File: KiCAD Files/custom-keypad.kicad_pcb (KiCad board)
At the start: 2 copper layers, 67.8 x 65.5 mm, 40 parts, among them IC1 AZ1117IH-3.3TRG1, IC2 USBLC6-2SC6, J1 UJ32-C-H-G-H2-SMT-TR, J2 EN11-HSM1BF20, J3 61300511121, SW1 SW_Push, SW2 SW_Push, SW3 SW_Push, SW4 SW_Push, SW8 SW_Push, SW9 SW_Push, U1 STM32H7A3RGTx, Y1 LFXTAL010595

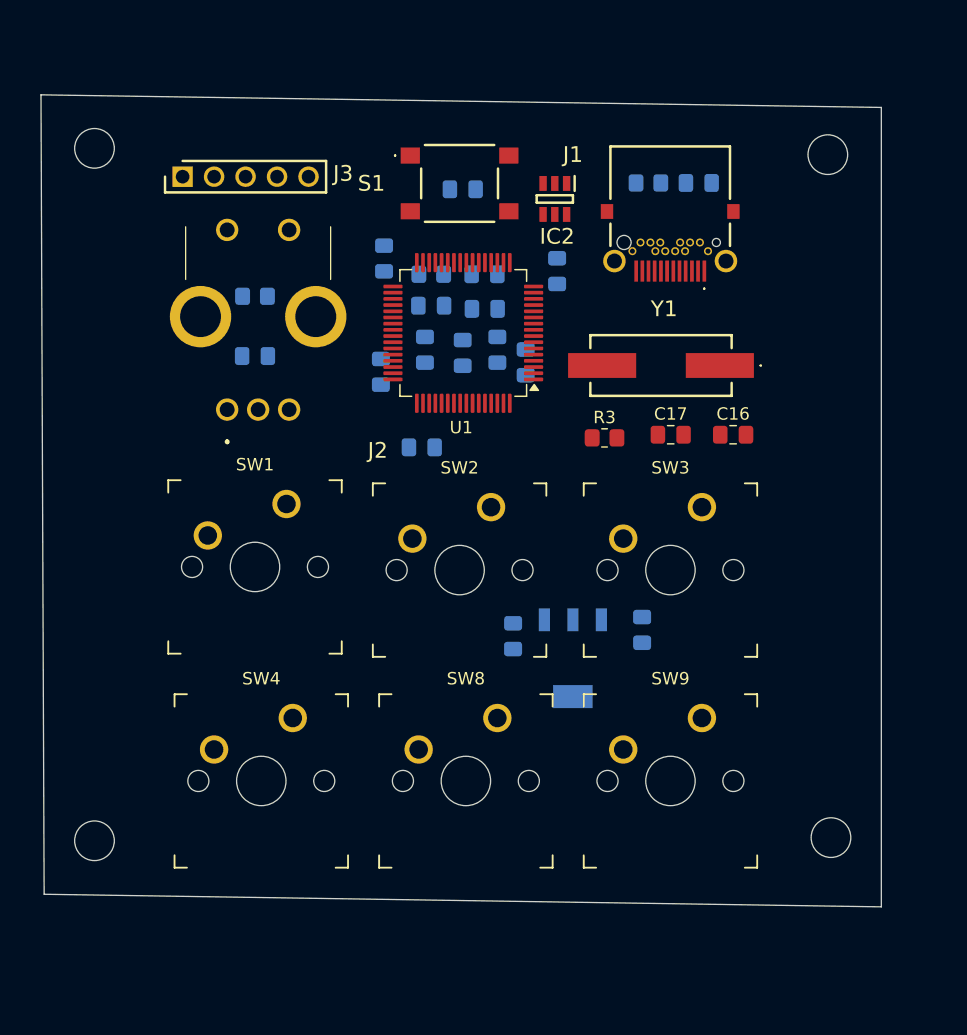
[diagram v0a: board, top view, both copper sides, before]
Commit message: improved PCB design and added debugging circuitry
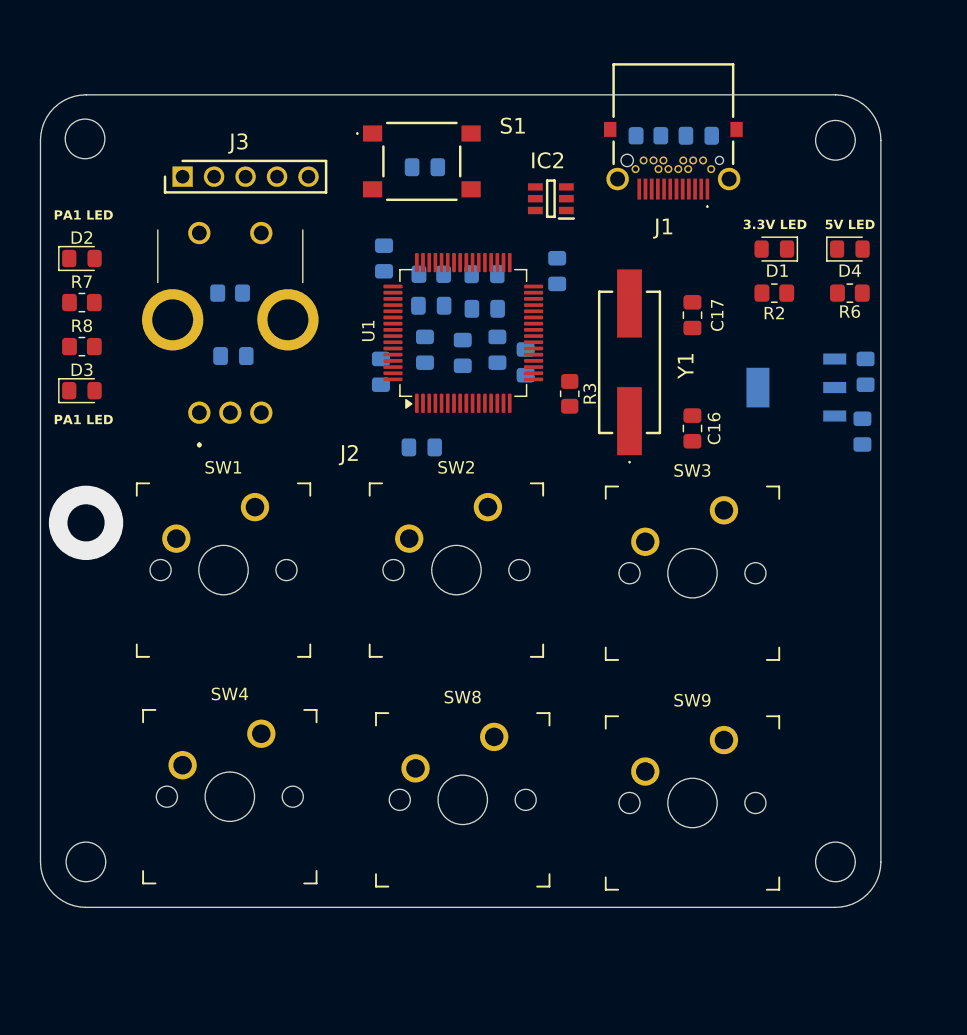
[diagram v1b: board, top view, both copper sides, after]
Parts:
- added D1: LED, LED_SMD:LED_0805_2012Metric_Pad1.15x1.40mm_HandSolder, F.Cu at (110.5, 38.1)
- added D2: LED, LED_SMD:LED_0805_2012Metric_Pad1.15x1.40mm_HandSolder, F.Cu at (54.6, 38.9)
- added D3: LED, LED_SMD:LED_0805_2012Metric_Pad1.15x1.40mm_HandSolder, F.Cu at (54.6, 49.5)
- added D4: LED, LED_SMD:LED_0805_2012Metric_Pad1.15x1.40mm_HandSolder, F.Cu at (116.6, 38.1)
- added R2: 220, Resistor_SMD:R_0805_2012Metric_Pad1.20x1.40mm_HandSolder, F.Cu at (110.5, 41.7)
- added R6: 330, Resistor_SMD:R_0805_2012Metric_Pad1.20x1.40mm_HandSolder, F.Cu at (116.6, 41.7)
- added R7: 220, Resistor_SMD:R_0805_2012Metric_Pad1.20x1.40mm_HandSolder, F.Cu at (54.6, 42.4)
- added R8: 220, Resistor_SMD:R_0805_2012Metric_Pad1.20x1.40mm_HandSolder, F.Cu at (54.6, 46.0)
- moved C14 32.7 mm to (117.6, 52.8)
- moved IC1 28.3 mm to (112.3, 49.3), turned to 180 degrees
- moved C13 27.6 mm to (117.9, 48.0), turned to 90 degrees
- moved C17 9.81 mm to (103.9, 43.4), turned to 90 degrees
- moved J1 6.62 mm to (102.3, 28.2)
- moved R3 4.53 mm to (94.0, 49.8), turned to -90 degrees
- moved C18 3.81 mm to (104.4, 29.0)
- moved R4 3.81 mm to (100.3, 29.0)
- moved S1 3.53 mm to (82.0, 31.0)
- moved C15 3.53 mm to (82.3, 31.5)
- moved C16 3.32 mm to (103.9, 52.6), turned to 90 degrees
- moved SW4 2.84 mm to (66.5, 82.3)
- moved Y1 2.55 mm to (98.8, 47.2), turned to 90 degrees
- moved SW1 2.55 mm to (66.0, 64.0)
- moved SW9 2.51 mm to (103.9, 82.8)
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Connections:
- C15 pad 1: nRST -> VBAT
- S1 pad 1: nRST -> VBAT
- U1 pad 7: nRST -> VBAT
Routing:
- net GND: vias 0 -> 1
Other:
- board size 67.8 x 65.5 mm -> 67.8 x 65.6 mm
- board text added: "3.3V LED"
- board text added: "5V LED"
- board text added: "PA1 LED"

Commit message: fixed some drc issues and updated pcb
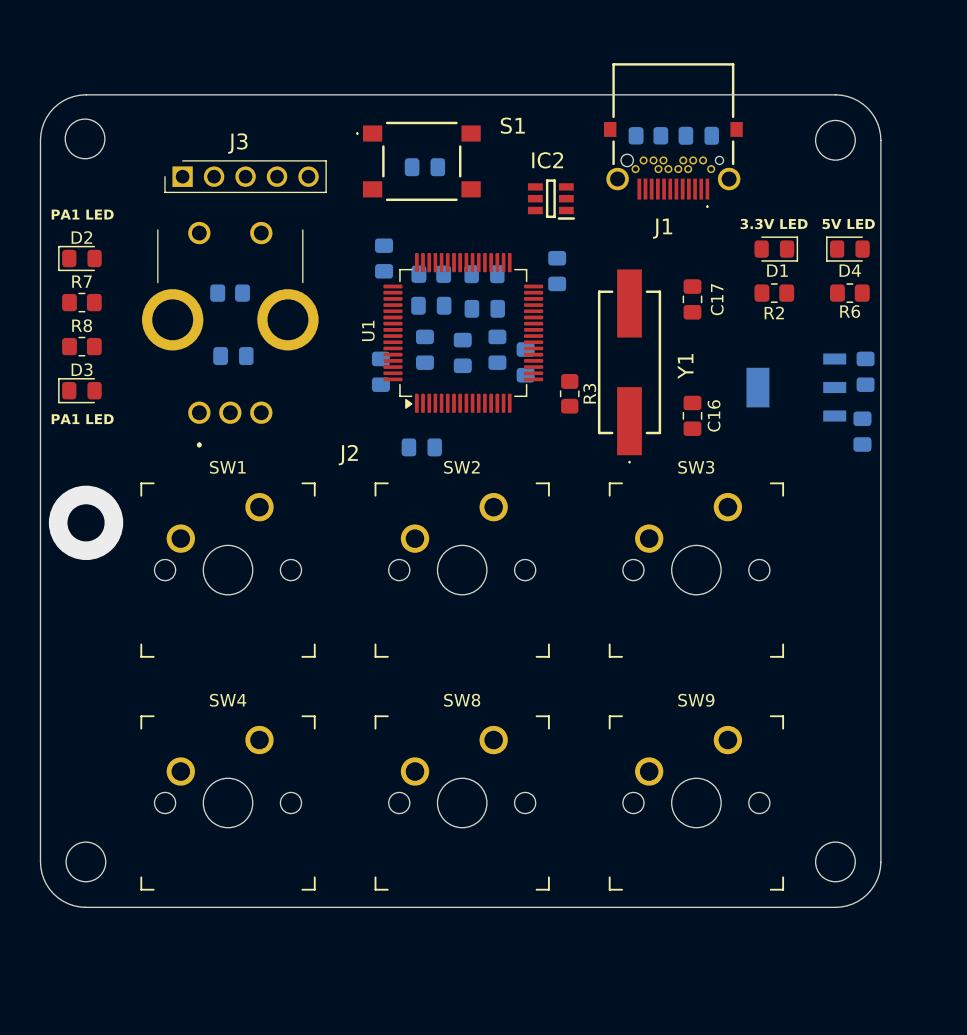
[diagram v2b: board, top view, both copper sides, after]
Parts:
- moved C17 1.27 mm to (103.9, 42.2)
- moved C16 1.02 mm to (103.9, 51.6)
- moved SW4 0.53 mm to (66.4, 82.8)
- moved SW2 0.47 mm to (85.3, 64.0)
- moved SW3 0.41 mm to (104.2, 64.0)
- moved SW1 0.36 mm to (66.4, 64.0)
- moved SW9 0.32 mm to (104.2, 82.8)
- moved SW8 0.26 mm to (85.3, 82.8)

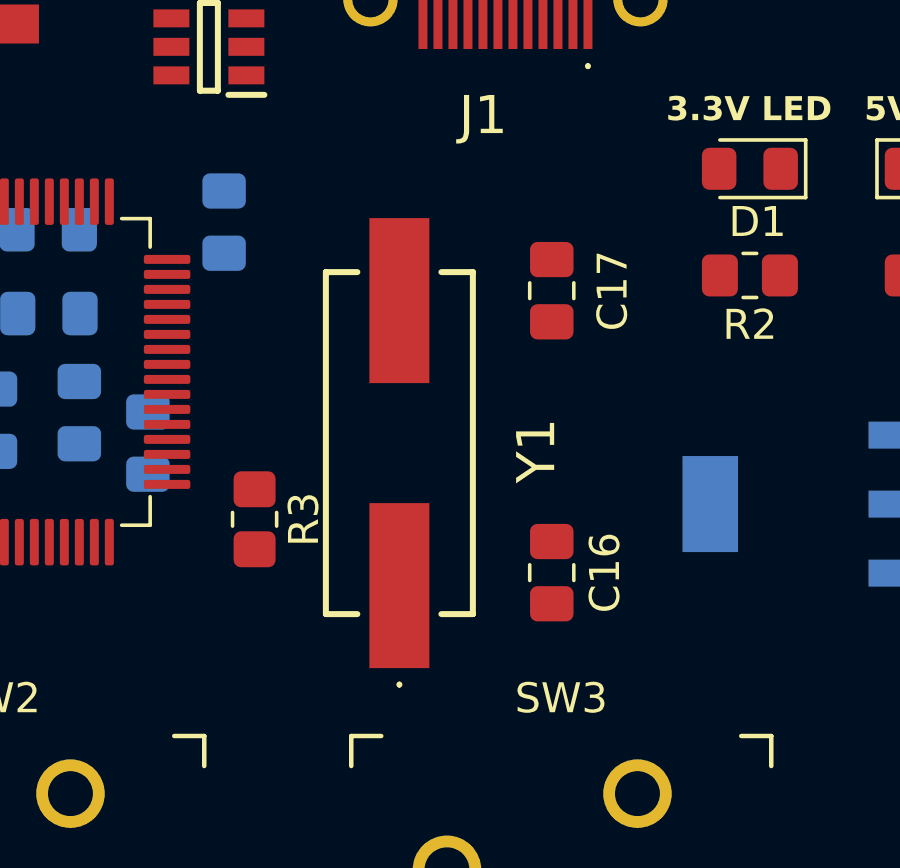
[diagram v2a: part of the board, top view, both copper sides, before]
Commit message: adjusted placement of oscillator
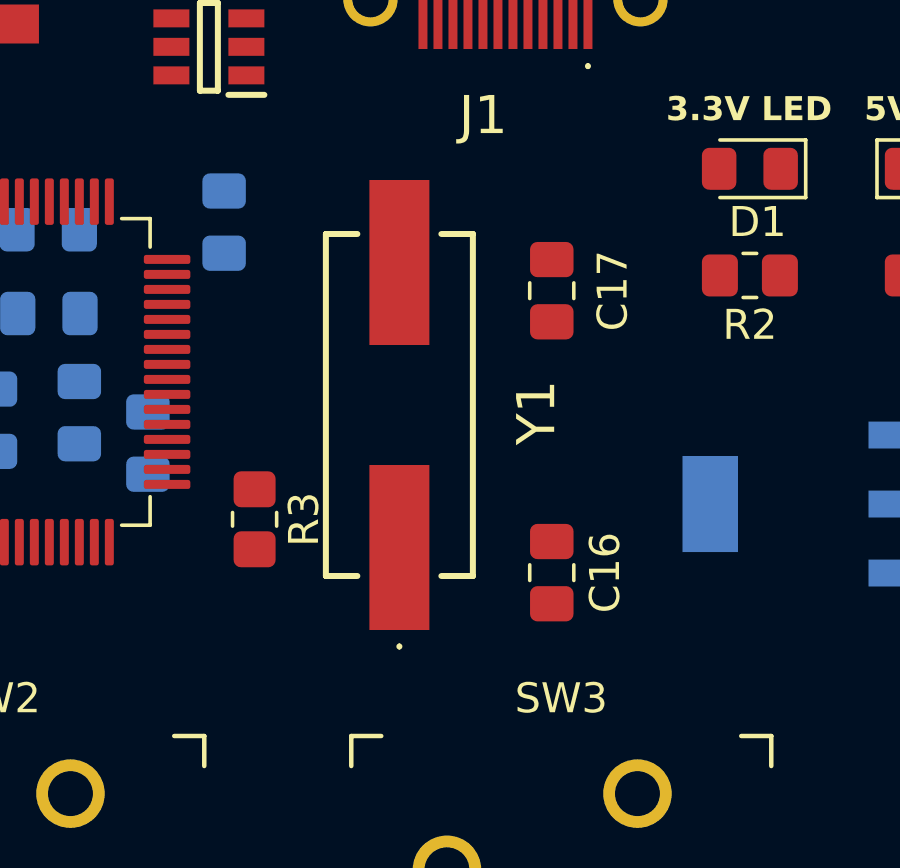
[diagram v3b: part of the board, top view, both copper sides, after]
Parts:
- moved Y1 1.27 mm to (98.8, 46.0)
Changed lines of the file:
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@@
 		(model "${KIPRJMOD}/3D Models/ImageToStl.com_Simple-CherryMX-Keycap.stp"
 			(offset
-				(xyz 1.5 2.5 10)
+				(xyz 1.5 2.5 5)
 			)
 			(scale
@@
 		(model "${KIPRJMOD}/3D Models/ImageToStl.com_Simple-CherryMX-Keycap.stp"
 			(offset
-				(xyz 1.5 2.5 10)
+				(xyz 1.5 2.5 5)
 			)
 			(scale
@@
 	(footprint "CustomFootprints:LFXTAL010595"
 		(layer "F.Cu")
-		(at 98.806 47.244 90)
+		(at 98.806 45.974 90)
 		(descr "11.40mm x 3.80mm x 4.9mm")
 		(tags "Crystal or Oscillator")
@@
 		(model "${KIPRJMOD}/3D Models/ImageToStl.com_Simple-CherryMX-Keycap.stp"
 			(offset
-				(xyz 1.5 2.5 10)
+				(xyz 1.5 2.5 5)
 			)
 			(scale
@@
 		(model "${KIPRJMOD}/3D Models/ImageToStl.com_Simple-CherryMX-Keycap.stp"
 			(offset
-				(xyz 1.5 2.5 10)
+				(xyz 1.5 2.5 5)
 			)
 			(scale
@@
 		(model "${KIPRJMOD}/3D Models/ImageToStl.com_Simple-CherryMX-Keycap.stp"
 			(offset
-				(xyz 1.5 2.5 10)
+				(xyz 1.5 2.5 5)
 			)
 			(scale
@@
 		(model "${KIPRJMOD}/3D Models/ImageToStl.com_Simple-CherryMX-Keycap.stp"
 			(offset
-				(xyz 1.5 2.5 10)
+				(xyz 1.5 2.5 5)
 			)
 			(scale

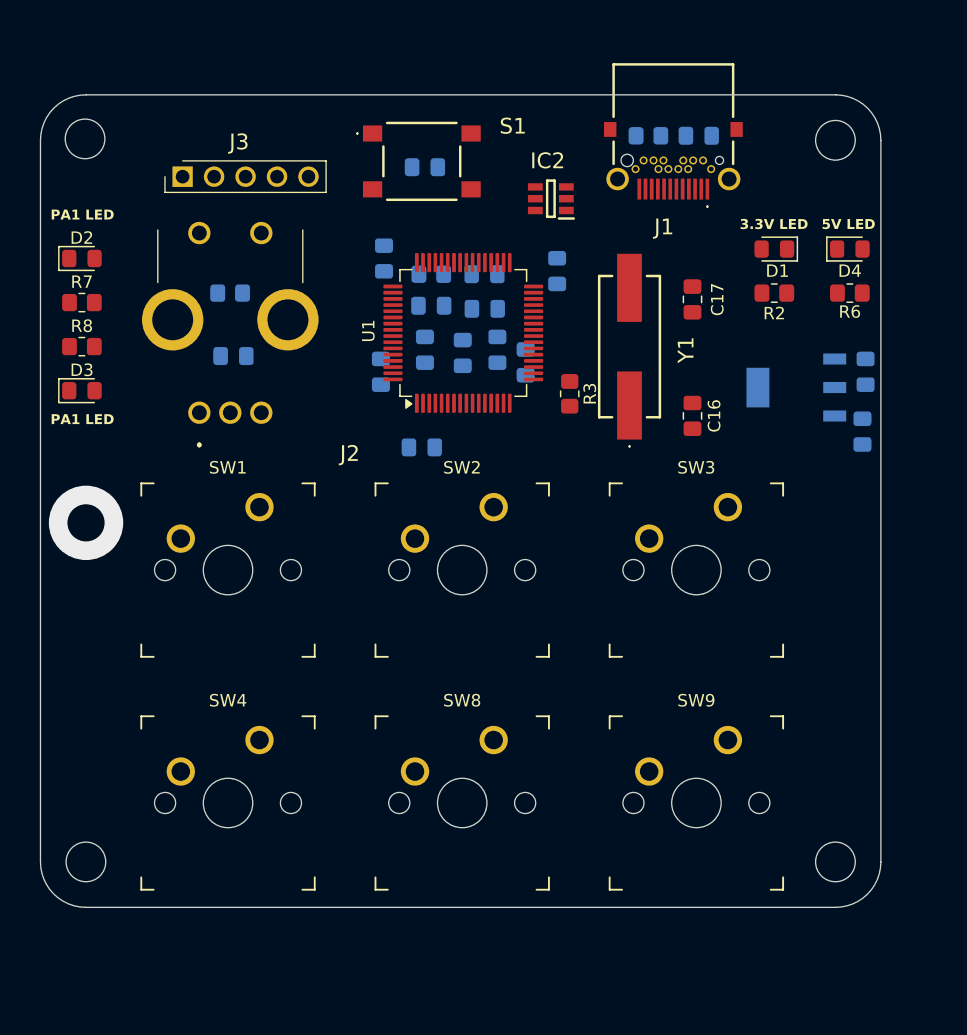
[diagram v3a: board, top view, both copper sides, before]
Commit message: finished pcb and diagram, need to double check before producing
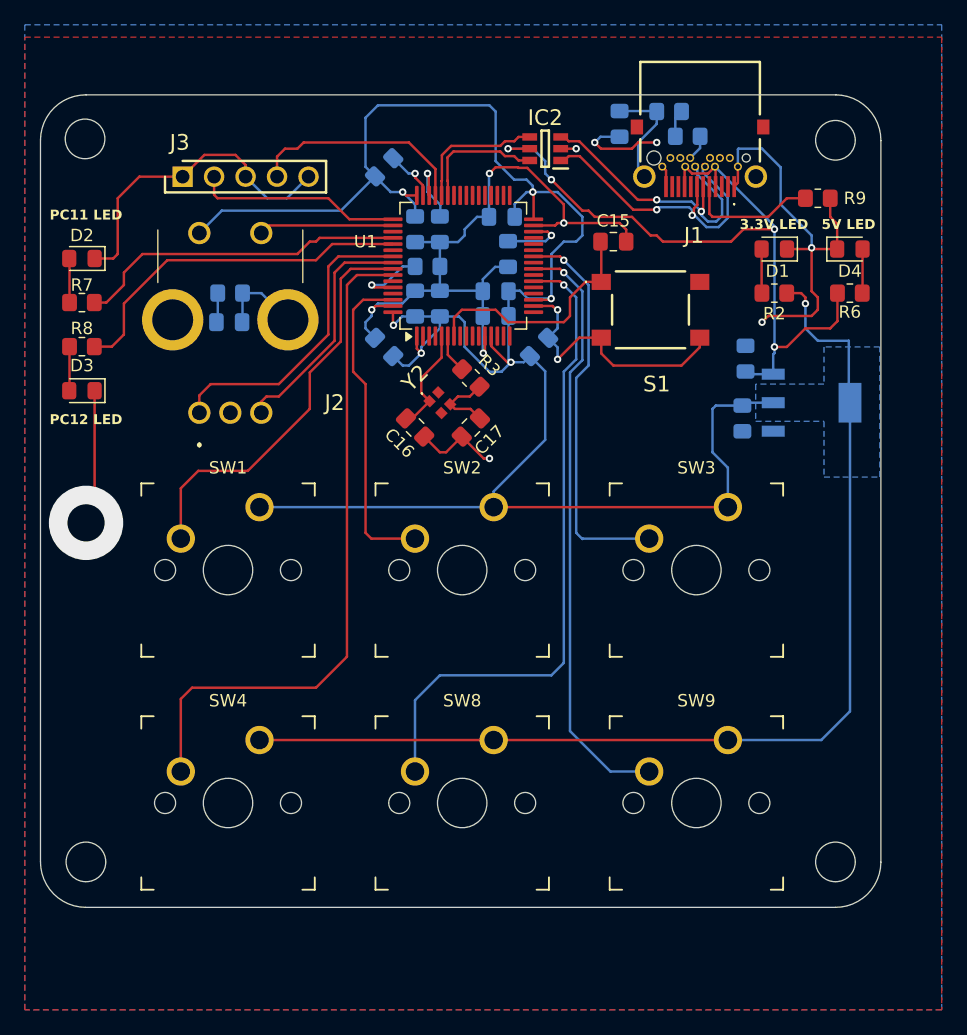
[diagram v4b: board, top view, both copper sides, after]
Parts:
- removed Y1: LFXTAL010595, CustomFootprints:LFXTAL010595
- added R10: 5.1k, Resistor_SMD:R_0805_2012Metric_Pad1.20x1.40mm_HandSolder, B.Cu at (103.5, 29.0)
- added R9: 5.1k, Resistor_SMD:R_0805_2012Metric_Pad1.20x1.40mm_HandSolder, F.Cu at (114.0, 34.0)
- added Y2: XRCGB25M000FAN00R0, CustomFootprints:XRCGB, F.Cu at (83.5, 50.5)
- C15: moved to F.Cu
- moved C1 22.8 mm to (79.0, 31.5), turned to 45 degrees
- moved C16 22.4 mm to (81.5, 52.5), turned to -45 degrees
- moved S1 22.0 mm to (100.5, 43.0)
- moved C17 20.7 mm to (86.0, 52.5), turned to -135 degrees
- moved C15 16.3 mm to (97.5, 37.5), turned to 0 degrees
- moved C10 12.9 mm to (91.5, 46.0), turned to 45 degrees
- moved C14 11.1 mm to (108.2, 46.9), turned to 90 degrees
- moved C6 10.7 mm to (81.5, 36.5)
- moved C13 10.6 mm to (107.9, 51.8), turned to -90 degrees
- moved C11 9.82 mm to (83.5, 42.5), turned to 90 degrees
- moved C5 9.80 mm to (83.5, 36.5)
- moved R3 8.08 mm to (86.0, 48.5), turned to 135 degrees
- moved C2 7.78 mm to (89.0, 38.5)
- moved C4 7.55 mm to (88.5, 35.5)
- moved C9 7.14 mm to (79.0, 46.0), turned to 135 degrees
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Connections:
- C15 pad 1: VBAT -> nRST
- J1 pad A5: unconnected-(J1-CC1-PadA5) -> Net-(J1-CC1)
- J1 pad B5: unconnected-(J1-CC2-PadB5) -> Net-(J1-CC2)
- J2 pad A1: PA1/Rotary A -> PB3/Rotary A
- J2 pad B1: PA1/Rotary B -> PB4/Rotary B
- J2 pad E1: PA1/Rotary SW -> PA15/Rotary SW
- R7 pad 1: PA1/Debug PA1 -> PC11/Debug PC11
- R8 pad 1: PA1/Debug PA2 -> PC12/Debug PC12
- S1 pad 1: VBAT -> nRST
- SW1 pad 2: PA1/Key 1 -> PB5/Key 1
- SW2 pad 2: PA1/Key 2 -> PB9/Key 2
- SW3 pad 2: PA1/Key 3 -> PB0/Key 3
- SW4 pad 2: PA1/Key 4 -> PB6/Key 4
- SW8 pad 2: PA1/Key 5 -> PA6/Key 5
- SW9 pad 2: PA1/Key 6 -> PC4/Key 6
- U1 pad 22: unconnected-(U1-PA6-Pad22) -> PA6/Key 5
- U1 pad 24: unconnected-(U1-PC4-Pad24) -> PC4/Key 6
- U1 pad 26: unconnected-(U1-PB0-Pad26) -> PB0/Key 3
- U1 pad 30: unconnected-(U1-VCAP-Pad30) -> VCAP1
- U1 pad 46: unconnected-(U1-VCAP-Pad46) -> VCAP2
- U1 pad 50: unconnected-(U1-PA15-Pad50) -> PA15/Rotary SW
- U1 pad 52: unconnected-(U1-PC11-Pad52) -> PC11/Debug PC11
- U1 pad 53: unconnected-(U1-PC12-Pad53) -> PC12/Debug PC12
- U1 pad 55: unconnected-(U1-PB3-Pad55) -> PB3/Rotary A
- U1 pad 56: unconnected-(U1-PB4-Pad56) -> PB4/Rotary B
- U1 pad 57: unconnected-(U1-PB5-Pad57) -> PB5/Key 1
- U1 pad 58: unconnected-(U1-PB6-Pad58) -> PB6/Key 4
- U1 pad 62: unconnected-(U1-PB9-Pad62) -> PB9/Key 2
- U1 pad 7: VBAT -> nRST
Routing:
- net VBAT: track 0.00 -> 255.6 mm, vias 0 -> 7
- net GND: track 0.00 -> 175.5 mm, vias 1 -> 14
- net +5V: track 0.00 -> 63.1 mm, vias 0 -> 4
- net PB6/Key 4: track 0.00 -> 54.7 mm
- net PA6/Key 5: track 0.00 -> 52.9 mm, vias 0 -> 1
- net PC4/Key 6: track 0.00 -> 48.3 mm, vias 0 -> 1
- net PB5/Key 1: track 0.00 -> 33.2 mm
- net PB0/Key 3: track 0.00 -> 31.9 mm, vias 0 -> 1
- net PC12/Debug PC12: track 0.00 -> 29.0 mm
- net PC11/Debug PC11: track 0.00 -> 26.9 mm
- net PB9/Key 2: track 0.00 -> 26.1 mm
- net D-: track 0.00 -> 24.9 mm, vias 0 -> 2
- net PB3/Rotary A: track 0.00 -> 24.9 mm
- net D+: track 0.00 -> 23.6 mm, vias 0 -> 2
- net nRST: track 0.00 -> 19.5 mm
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- added copper zone on B.Cu, net GND
- added copper zone on F.Cu, net PB3/Rotary A
- added copper zone on B.Cu, net VBAT
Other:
- board text added: "PC11 LED"
- board text added: "PC12 LED"
- board text removed: "PA1 LED"
